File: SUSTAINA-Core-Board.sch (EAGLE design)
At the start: 67 parts, among them IC1 LTC4418IUF, M1 POWER-MONITOR-MODULE, M2 POWER-MONITOR-MODULE, M3 BUCK-BOOST-SWITCH-MODE-POWER-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, M4 POWER-MONITOR-MODULE, M5 POWER-MONITOR-MODULE, Q1 SUM110P06-08L-E3, Q2 SUM110P06-08L-E3, Q3 SUM110P06-08L-E3, Q4 SUM110P06-08L-E3, Q5 SUM110P06-08L-E3, Q6 SUM110P06-08L-E3

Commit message: Upload data for RoboCup2023 competition specifications
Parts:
- added LED5: Green, led:LEDSML0603
- added R19: 2k, rcl:R-US_R0603
- C10, C9: value 0.1u -> 1u
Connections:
- net +ACTUATOR_POWER renamed +ACTR_PWR
- net +ACTUATOR_POWER_INPUT renamed +ACTR_PWR_INPUT
- net +ACTUATOR_SENSING renamed +ACTR_SENSING
- net +BATTERY_INPUT1 renamed +BATT_INPUT1
- net +BATTERY_INPUT1_FUSE renamed +BATT_INPUT1_FUSE
- net +BATTERY_INPUT2 renamed +BATT_INPUT2
- net +BATTERY_INPUT2_FUSE renamed +BATT_INPUT2_FUSE
- net +BATTERY_INPUT_SENSING1 renamed +BATT_INPUT_SENSING1
- net +BATTERY_INPUT_SENSING2 renamed +BATT_INPUT_SENSING2
- net +POWER_INPUT renamed +PWR_INPUT
- net +SBC_POWER renamed +SBC_PWR
- net +SBC_POWER_INPUT renamed +SBC_PWR_INPUT
- net +SBC_POWER_OUTPUT renamed +SBC_PWR_OUTPUT
- net GATE_ACTUATOR renamed GATE_ACTR
- net GATE_ACTUATOR_ renamed GATE_ACTR_
- new net LED_3V3: LED5.A, R19.1
- net +3V3: now also R19.2
- net GND: now also LED5.C
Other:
- note added: "Actuator Power & Signal Output"
- note added: "Actuator Signal Input"
- note added: "Actuator's Power Sensing"
- note added: "Fuse for short circuit (20A)"
- note added: "Fuse for short circuit (7.5A)"
- note added: "June 12, 2023"
- note added: "LED for checking the operation"
- note added: "Power Input & Sensing"
- note added: "Power Monitor"
- note added: "Power On/Off Switching"
- note added: "Power Sensing"
- note added: "Power Supply"
- note added: "Power Switching"
- note added: "Single Board Computer's Power Sensing"
- note removed: "Fuse for short circuit in Battery line (20A)"
- note removed: "Fuse for short circuit in CPU power line (2A)"
- note removed: "Fuse for short circuit in Servo power line (20A)"
- note removed: "Fuse for short circuit in Switching power line (20A)"
- note removed: "June 1, 2023"
- note removed: "LED for checking the operation Actuator Power"
- note removed: "LED for checking the operation Battery line"
- note removed: "LED for checking the operation Buck-Boost Converter and FUSE"
- note removed: "LED for checking the operation Switching Power line"
- moved on the sheet: C10, C11, C12, C13, C14, C9, CH10, CH11, CH12, CH13, CH4, CH5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

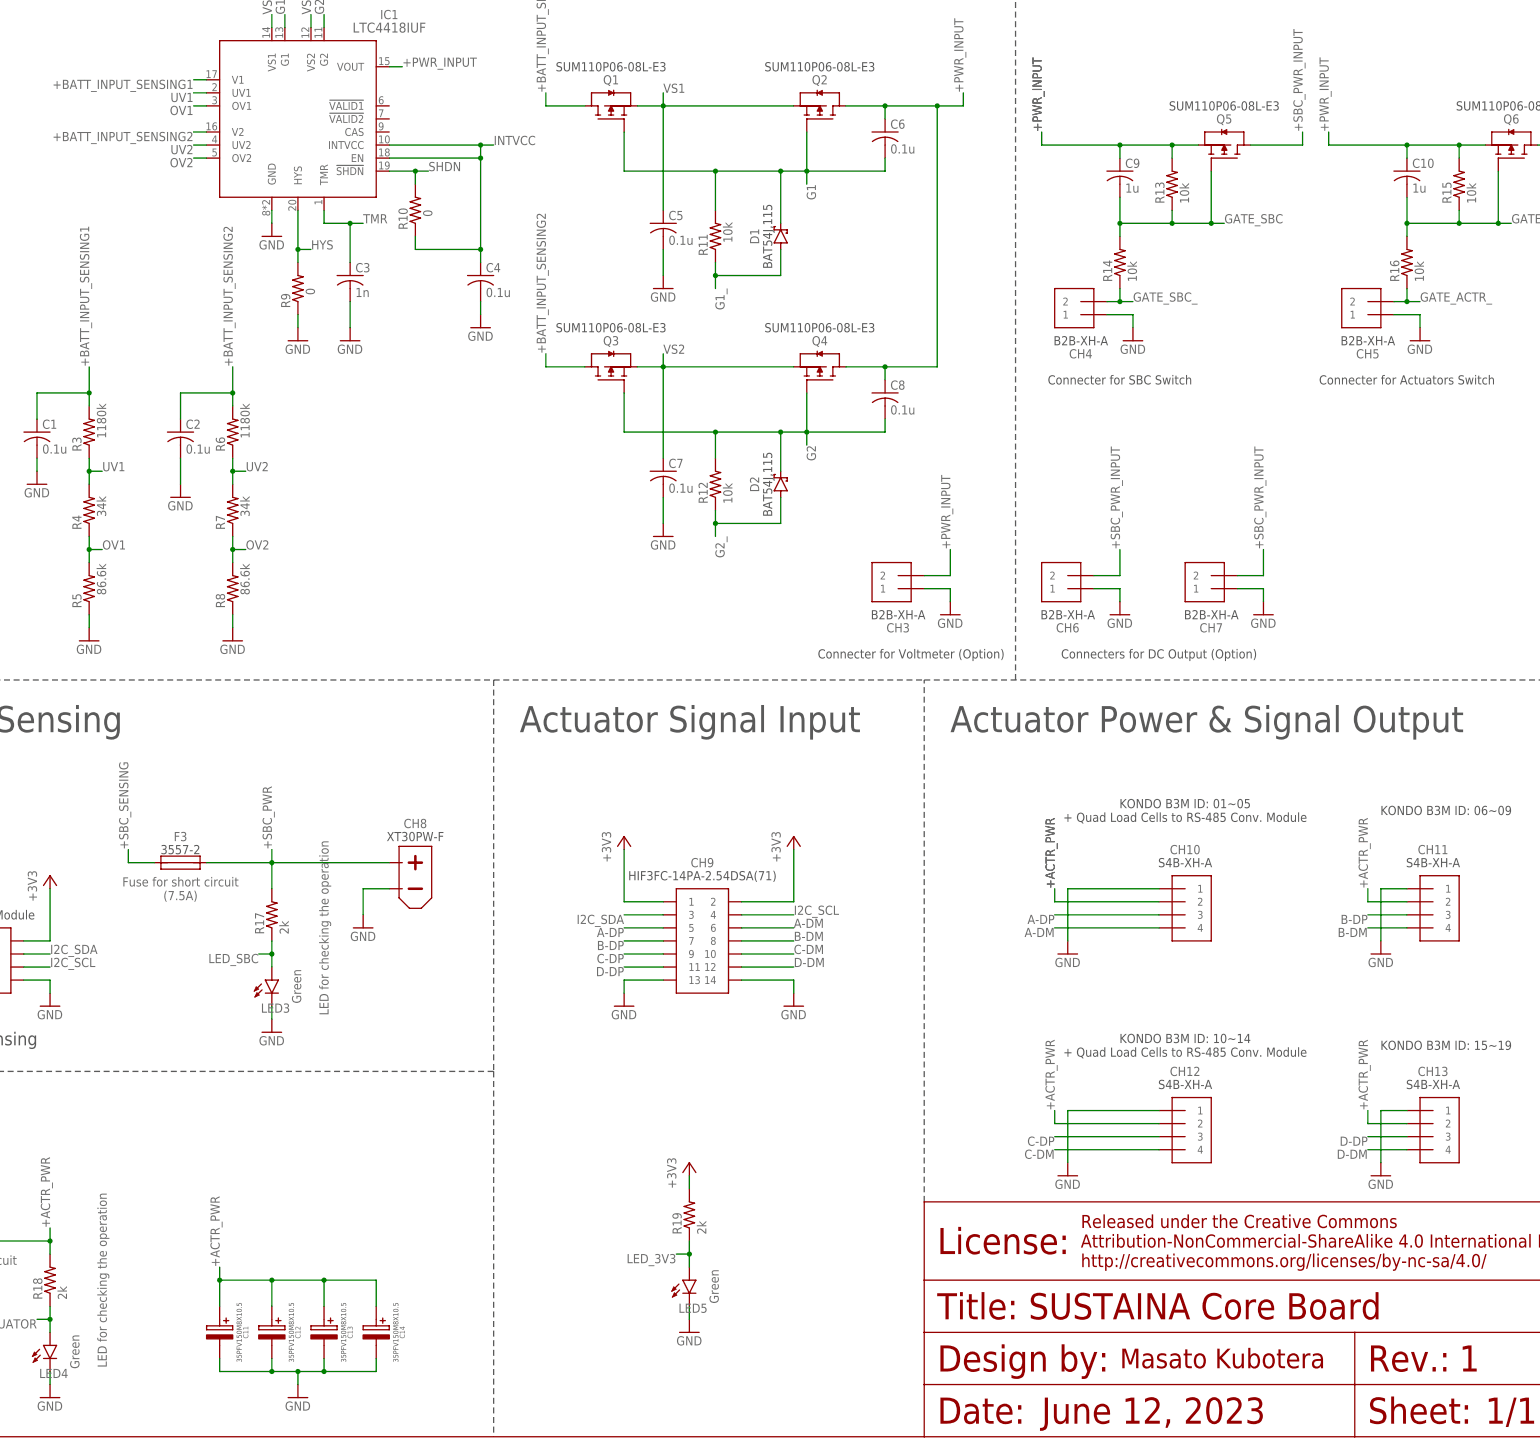
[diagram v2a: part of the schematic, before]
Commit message: Solved the problem of not being able to use a switching power supply in Rev.1
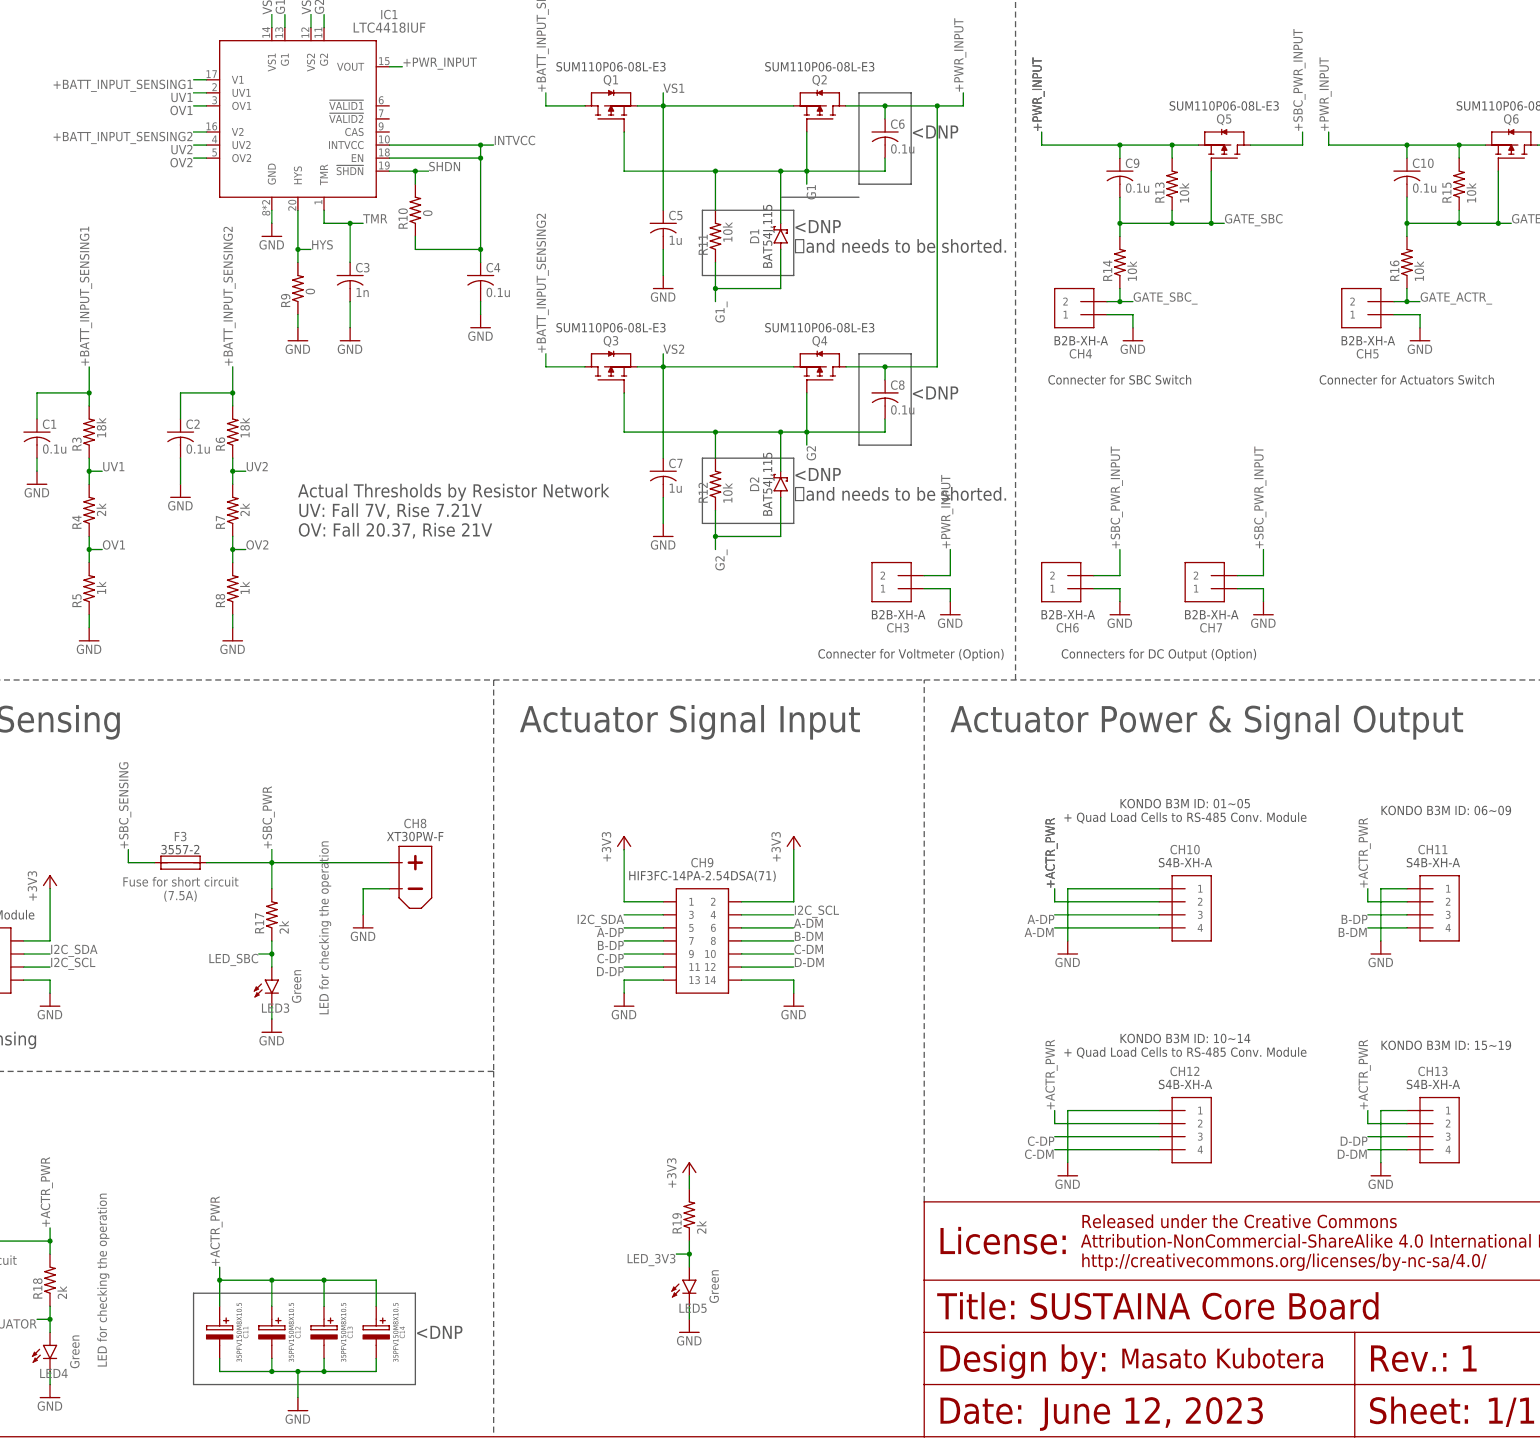
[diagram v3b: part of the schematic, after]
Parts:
- C10, C9: value 1u -> 0.1u
- C5, C7: value 0.1u -> 1u
- R3, R6: value 1180k -> 18k
- R4, R7: value 34k -> 2k
- R5, R8: value 86.6k -> 1k
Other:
- note added: "<DNP"
- note added: "<DNP and needs to be shorted."
- note added: "Actual Thresholds by Resistor Network UV: Fall 7V, Rise 7.21V OV: Fall 20.37, Rise 21V"

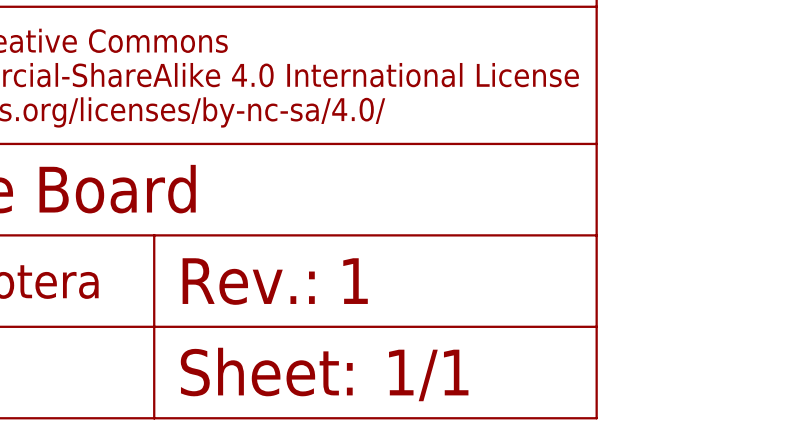
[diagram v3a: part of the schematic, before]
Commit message: Changed the version of schematic to 1.1
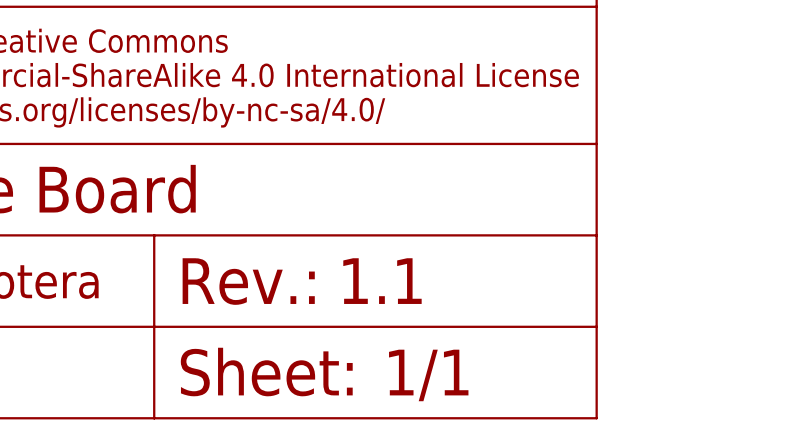
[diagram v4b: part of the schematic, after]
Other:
- note added: "1.1"
- note removed: "1"
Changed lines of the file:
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@@
 <text x="284.48" y="152.4" size="1.778" layer="97" ratio="10" align="center">Connecter for Voltmeter (Option)</text>
 <wire x1="287.02" y1="45.72" x2="287.02" y2="147.32" width="0.1524" layer="97" style="longdash"/>
-<text x="391.16" y="15.24" size="5.08" layer="94" ratio="10" align="center-left">1</text>
+<text x="391.16" y="15.24" size="5.08" layer="94" ratio="10" align="center-left">1.1</text>
 <text x="396.24" y="5.08" size="5.08" layer="94" ratio="10" align="center-left">1/1</text>
 <text x="309.88" y="5.08" size="5.08" layer="94" ratio="10" align="center-left">June 12, 2023</text>
